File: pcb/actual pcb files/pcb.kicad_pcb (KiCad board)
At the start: 2 copper layers, 84 x 79 mm, 21 parts, among them J1 Conn_01x04_Pin, SW1 SW_Push, SW10 RotaryEncoder_Switch, SW2 SW_Push, SW3 SW_Push, SW4 SW_Push, SW5 SW_Push, SW6 SW_Push, SW7 SW_Push, SW8 SW_Push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

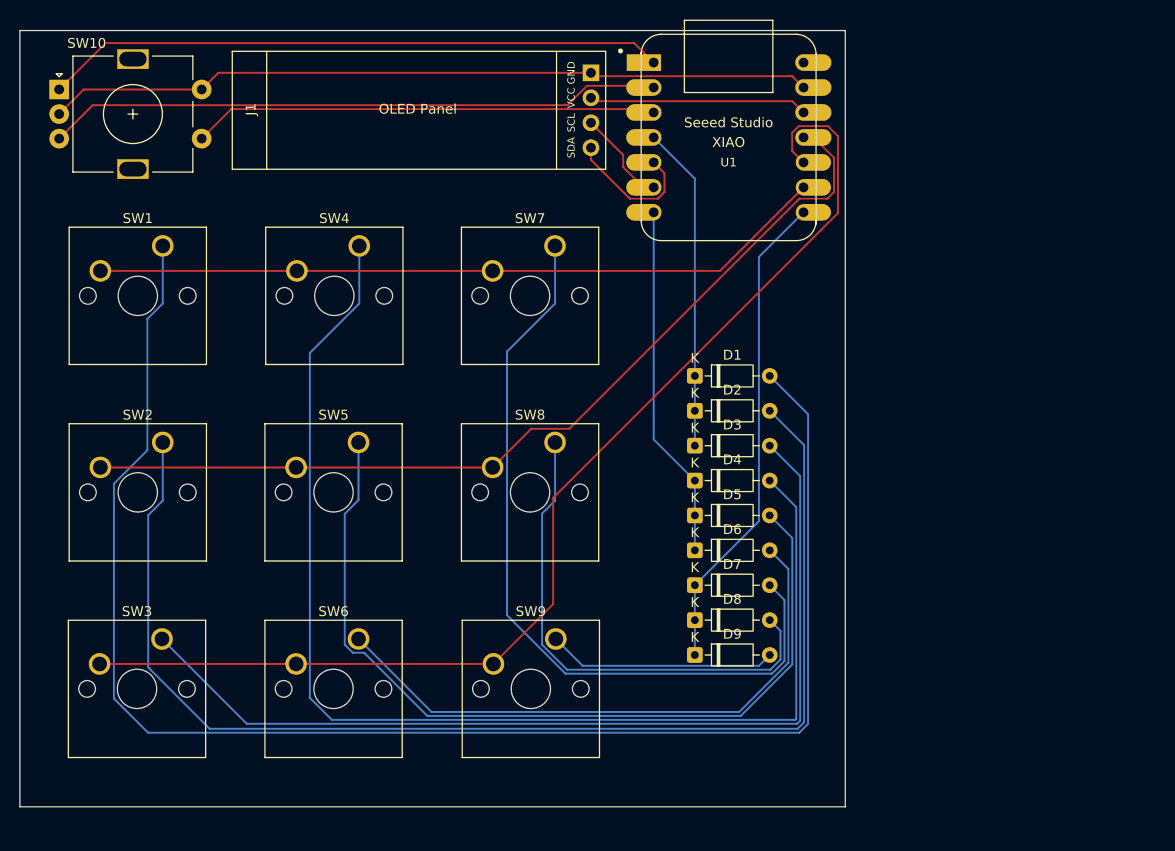
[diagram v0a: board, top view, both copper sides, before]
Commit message: editted PCB
- added fillets
- added a silkscreen
- COMPANY NAME = MASCOORP
- rewired
- fixed switch spacing
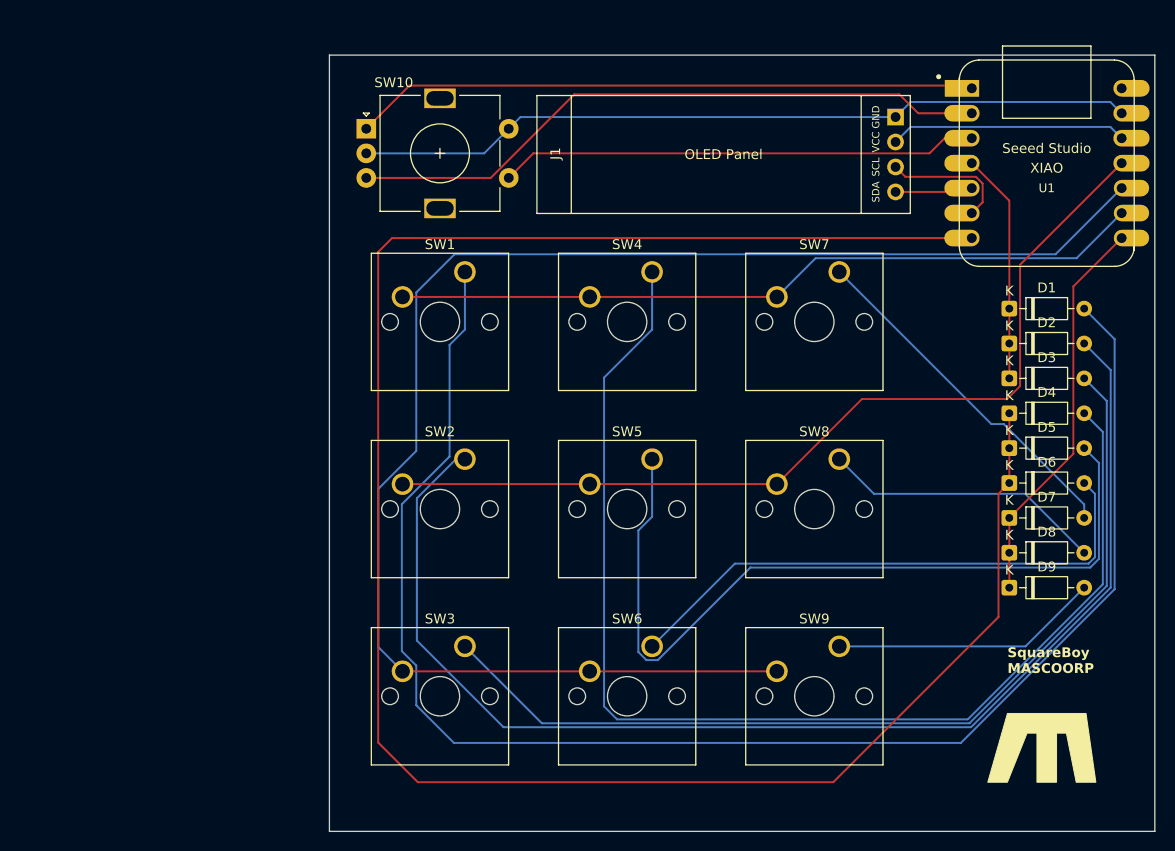
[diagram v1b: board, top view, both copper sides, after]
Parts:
- moved D1 32.7 mm to (153.2, 55.8)
- moved D2 32.7 mm to (153.2, 59.4)
- moved D3 32.7 mm to (153.2, 62.9)
- moved D6 32.7 mm to (153.2, 73.5)
- moved D7 32.7 mm to (153.2, 77.1)
- moved D4 32.7 mm to (153.2, 66.5)
- moved D5 32.7 mm to (153.2, 70.0)
- moved D8 32.7 mm to (153.2, 80.7)
- moved D9 32.7 mm to (153.2, 84.2)
- moved U1 32.5 mm to (157.0, 41.0)
- moved SW10 31.5 mm to (87.8, 37.5)
- moved J1 31.3 mm to (105.1, 34.1)
- moved SW1 30.9 mm to (97.8, 52.1)
- moved SW3 30.8 mm to (97.8, 90.2)
- moved SW2 30.8 mm to (97.8, 71.1)
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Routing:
- net Net-(D4-K): track 36.1 -> 203.9 mm
- net Net-(D7-A): track 79.2 -> 36.1 mm
- net Net-(U1-PA5_A9_D9_MISO): track 117.2 -> 155.5 mm
- net Net-(D8-A): track 51.3 -> 28.9 mm
- net Net-(D1-K): track 33.1 -> 23.5 mm
- net Net-(D7-K): track 49.6 -> 40.3 mm
- net Net-(J1-Pin_4): track 14.1 -> 7.92 mm
- net Net-(D5-A): track 88.0 -> 83.6 mm
- net Net-(D6-A): track 61.1 -> 56.8 mm
- net Net-(D9-A): track 23.4 -> 27.4 mm
- net Net-(J1-Pin_3): track 9.83 -> 13.0 mm
- net Net-(U1-PA4_A1_D1): track 62.8 -> 65.9 mm
- net Net-(D4-A): track 123.9 -> 121.4 mm
- net Net-(J1-Pin_2): track 22.3 -> 24.1 mm
- net Net-(U1-PA7_A8_D8_SCK): track 75.1 -> 76.7 mm
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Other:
- board text added: "SquareBoy MASCOORP"
